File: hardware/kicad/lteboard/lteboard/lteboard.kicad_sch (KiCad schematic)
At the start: 0 parts

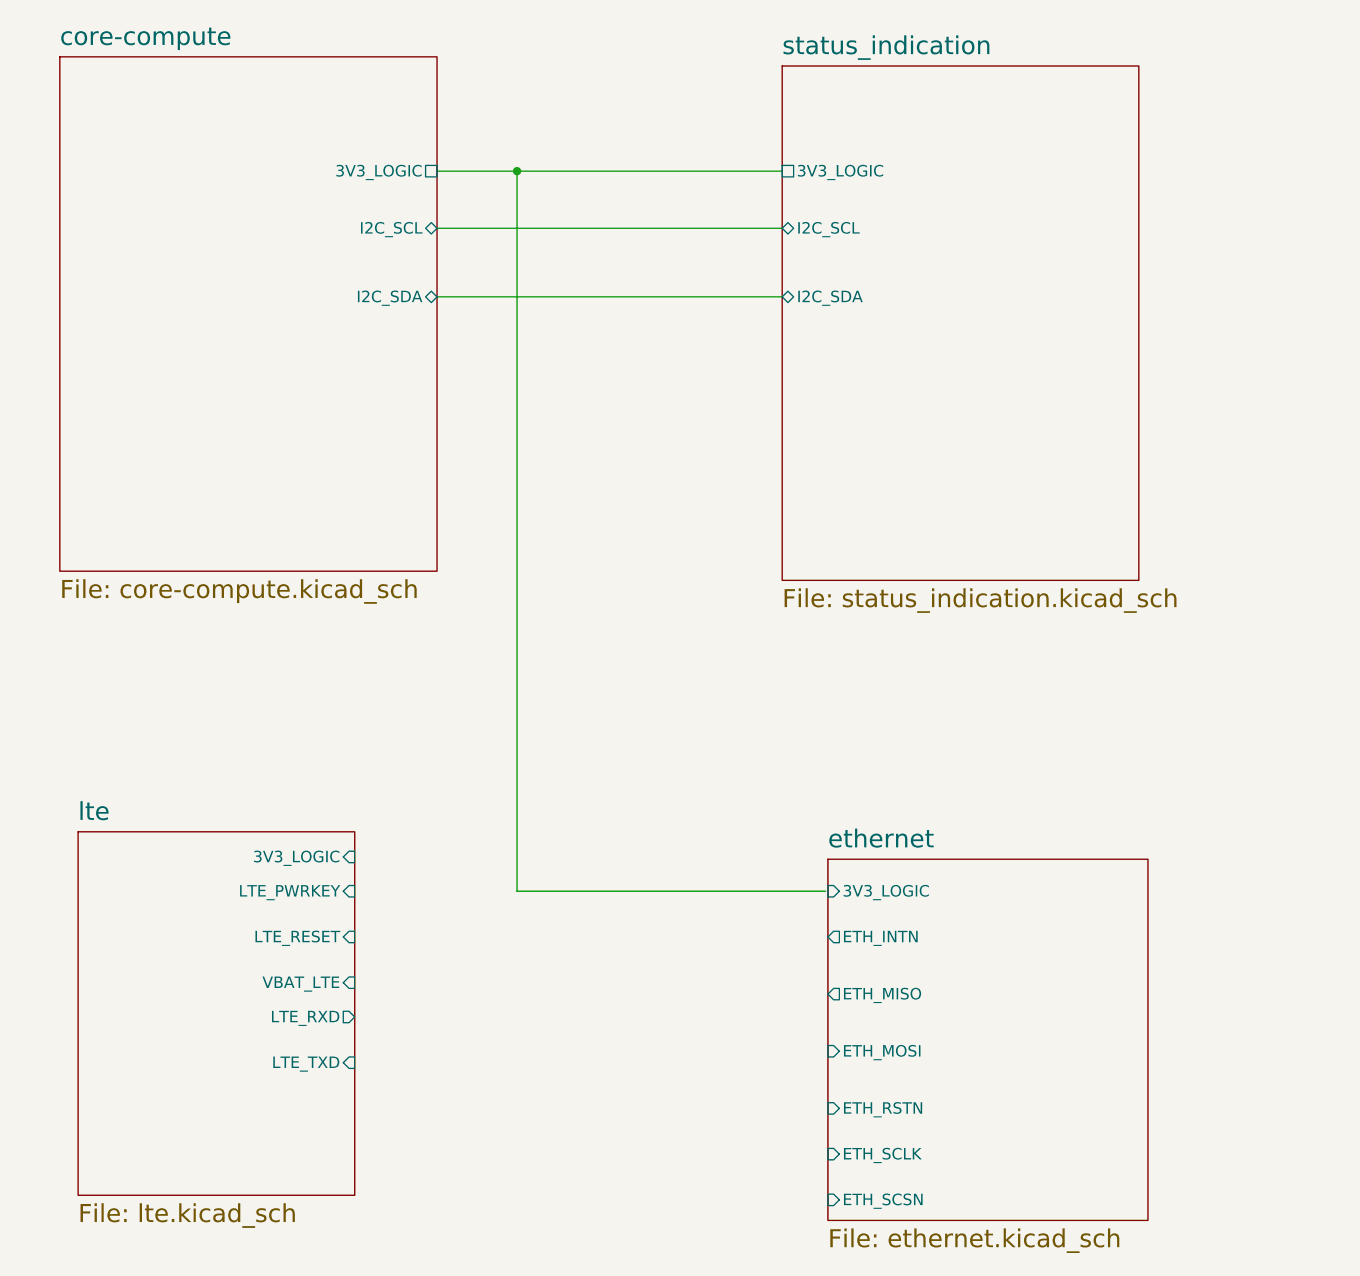
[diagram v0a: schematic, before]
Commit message: Merge ioboard and lteboard into one schematic project named ioboard+lteboard
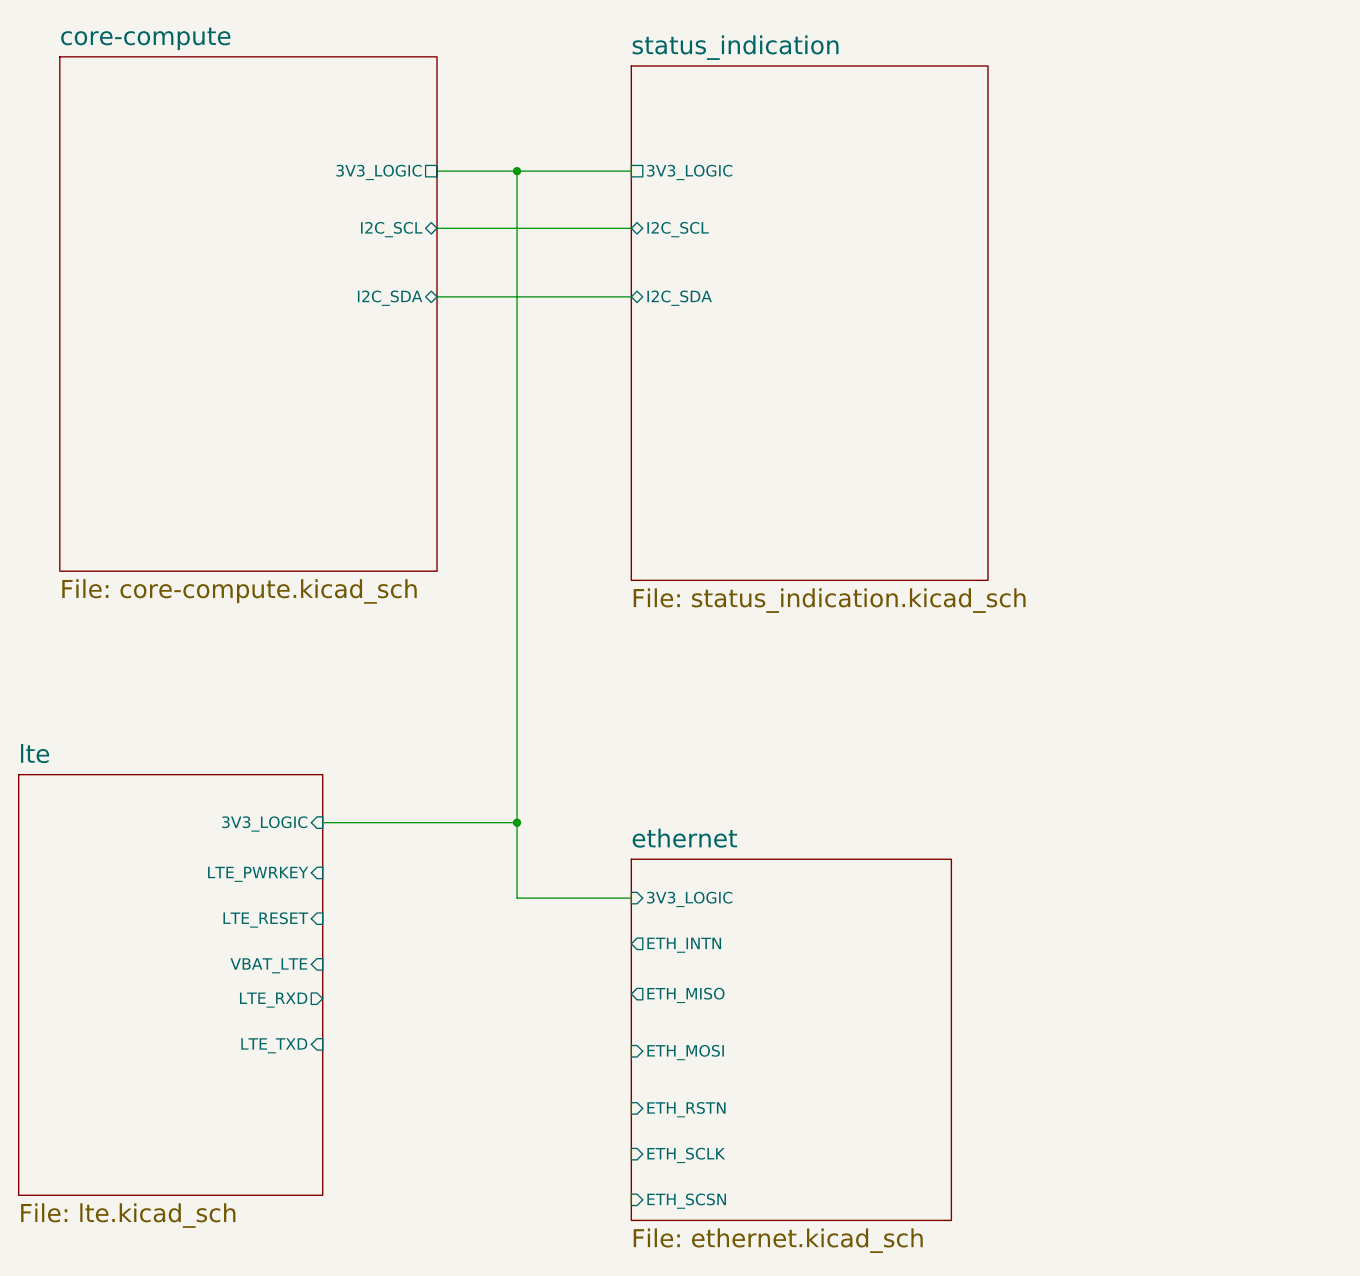
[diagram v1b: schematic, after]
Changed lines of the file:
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@@
 	(paper "A4")
+	(junction
+		(at 86.36 123.19)
+		(diameter 0)
+		(color 0 0 0 0)
+	)
 	(junction
 		(at 86.36 50.8)
@@
 	(wire
 		(pts
-			(xy 86.36 130.81) (xy 86.36 50.8)
+			(xy 86.36 50.8) (xy 86.36 123.19)
+		)
+		(stroke
+			(width 0)
+			(type default)
+		)
+	)
+	(wire
+		(pts
+			(xy 64.77 123.19) (xy 86.36 123.19)
 		)
 		(stroke
@@
 	(wire
 		(pts
-			(xy 86.36 130.81) (xy 120.65 130.81)
-		)
-		(stroke
-			(width 0)
-			(type default)
-		)
-	)
-	(wire
-		(pts
-			(xy 77.47 64.77) (xy 115.824 64.77)
-		)
-		(stroke
-			(width 0)
-			(type default)
-		)
-	)
-	(wire
-		(pts
-			(xy 86.36 50.8) (xy 115.824 50.8)
-		)
-		(stroke
-			(width 0)
-			(type default)
-		)
-	)
-	(wire
-		(pts
-			(xy 77.47 57.15) (xy 115.824 57.15)
+			(xy 86.36 131.572) (xy 99.06 131.572)
+		)
+		(stroke
+			(width 0)
+			(type default)
+		)
+	)
+	(wire
+		(pts
+			(xy 77.47 64.77) (xy 99.06 64.77)
+		)
+		(stroke
+			(width 0)
+			(type default)
+		)
+	)
+	(wire
+		(pts
+			(xy 86.36 50.8) (xy 99.06 50.8)
+		)
+		(stroke
+			(width 0)
+			(type default)
+		)
+	)
+	(wire
+		(pts
+			(xy 77.47 57.15) (xy 99.06 57.15)
+		)
+		(stroke
+			(width 0)
+			(type default)
+		)
+	)
+	(wire
+		(pts
+			(xy 86.36 123.19) (xy 86.36 131.572)
 		)
 		(stroke
@@
 	)
 	(sheet
-		(at 37.592 124.206)
-		(size 30.734 40.386)
+		(at 30.988 117.856)
+		(size 33.782 46.736)
 		(exclude_from_sim no)
 		(in_bom yes)
@@
 		)
 		(property "Sheetname" "lte"
-			(at 37.592 123.1294 0)
+			(at 30.988 116.7794 0)
 			(effects
 				(font
@@
 		)
 		(property "Sheetfile" "lte.kicad_sch"
-			(at 37.592 165.4686 0)
+			(at 30.988 165.4686 0)
 			(effects
 				(font
@@
 		)
 		(pin "3V3_LOGIC" input
-			(at 68.326 127 0)
+			(at 64.77 123.19 0)
 			(effects
 				(font
@@
 		)
 		(pin "LTE_PWRKEY" input
-			(at 68.326 130.81 0)
+			(at 64.77 128.778 0)
 			(effects
 				(font
@@
 		)
 		(pin "LTE_RESET" input
-			(at 68.326 135.89 0)
+			(at 64.77 133.858 0)
 			(effects
 				(font
@@
 		)
 		(pin "VBAT_LTE" input
-			(at 68.326 140.97 0)
+			(at 64.77 138.938 0)
 			(effects
 				(font
@@
 		)
 		(pin "LTE_RXD" output
-			(at 68.326 144.78 0)
+			(at 64.77 142.748 0)
 			(effects
 				(font
@@
 		)
 		(pin "LTE_TXD" input
-			(at 68.326 149.86 0)
+			(at 64.77 147.828 0)
 			(effects
 				(font
@@
 	)
 	(sheet
-		(at 120.904 127.254)
+		(at 99.06 127.254)
 		(size 35.56 40.132)
 		(exclude_from_sim no)
@@
 		)
 		(property "Sheetname" "ethernet"
-			(at 120.904 126.1774 0)
+			(at 99.06 126.1774 0)
 			(effects
 				(font
@@
 		)
 		(property "Sheetfile" "ethernet.kicad_sch"
-			(at 120.904 168.2626 0)
+			(at 99.06 168.2626 0)
 			(effects
 				(font
@@
 		)
 		(pin "3V3_LOGIC" input
-			(at 120.904 130.81 180)
+			(at 99.06 131.572 180)
 			(effects
 				(font
@@
 		)
 		(pin "ETH_INTN" output
-			(at 120.904 135.89 180)
+			(at 99.06 136.652 180)
 			(effects
 				(font
@@
 		)
 		(pin "ETH_MISO" output
-			(at 120.904 142.24 180)
+			(at 99.06 142.24 180)
 			(effects
 				(font
@@
 		)
 		(pin "ETH_MOSI" input
-			(at 120.904 148.59 180)
+			(at 99.06 148.59 180)
 			(effects
 				(font
@@
 		)
 		(pin "ETH_RSTN" input
-			(at 120.904 154.94 180)
+			(at 99.06 154.94 180)
 			(effects
 				(font
@@
 		)
 		(pin "ETH_SCLK" input
-			(at 120.904 160.02 180)
+			(at 99.06 160.02 180)
 			(effects
 				(font
@@
 		)
 		(pin "ETH_SCSN" input
-			(at 120.904 165.1 180)
+			(at 99.06 165.1 180)
 			(effects
 				(font
@@
 	)
 	(sheet
-		(at 115.824 39.116)
+		(at 99.06 39.116)
 		(size 39.624 57.15)
 		(exclude_from_sim no)
@@
 		)
 		(property "Sheetname" "status_indication"
-			(at 115.824 38.0394 0)
+			(at 99.06 38.0394 0)
 			(effects
 				(font
@@
 		)
 		(property "Sheetfile" "status_indication.kicad_sch"
-			(at 115.824 97.1426 0)
+			(at 99.06 97.1426 0)
 			(effects
 				(font
@@
 		)
 		(pin "3V3_LOGIC" passive
-			(at 115.824 50.8 180)
+			(at 99.06 50.8 180)
 			(effects
 				(font
@@
 		)
 		(pin "I2C_SCL" bidirectional
-			(at 115.824 57.15 180)
+			(at 99.06 57.15 180)
 			(effects
 				(font
@@
 		)
 		(pin "I2C_SDA" bidirectional
-			(at 115.824 64.77 180)
-			(effects
-				(font
+			(at 99.06 64.77 180)
+			(effects
+				(font
